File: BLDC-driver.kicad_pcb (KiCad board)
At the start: 2 copper layers, 52.2 x 52.2 mm, 105 parts, among them J1 Conn_01x06, J2 Conn_01x06, Q1 FDMS8018, Q2 FDMS8018, Q3 FDMS8018, Q4 FDMS8018, Q5 FDMS8018, Q6 FDMS8018, Q7 BC807, U1 NCP81151B, U11 SN75176AD, U2 STM32L412CB, U4 NCP81151B, U5 NCP81151B, U6 MP2359, U7 MIC5504-3.3YM5, U8 NCS213RSQT2G, U9 NCS213RSQT2G, Y1 8MHz

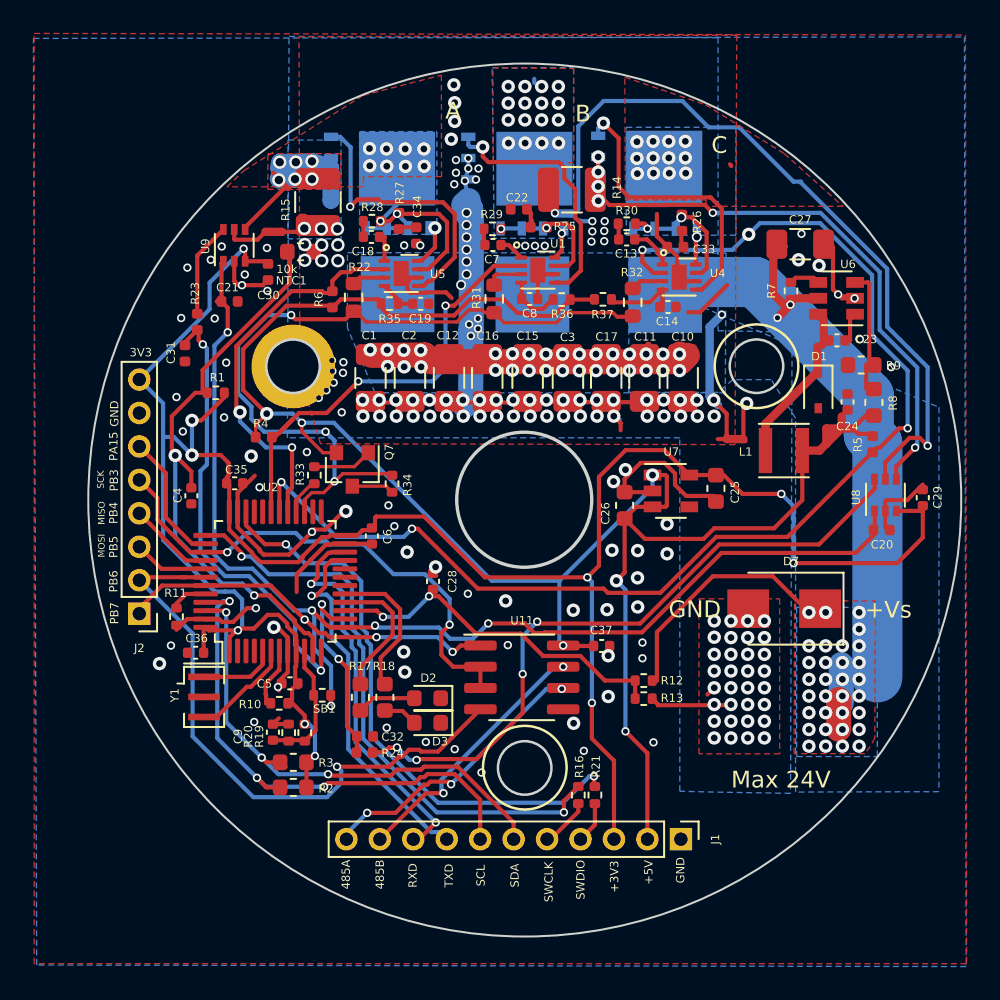
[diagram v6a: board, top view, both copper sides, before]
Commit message: Rev3: Update connectors, add JST PH connectors
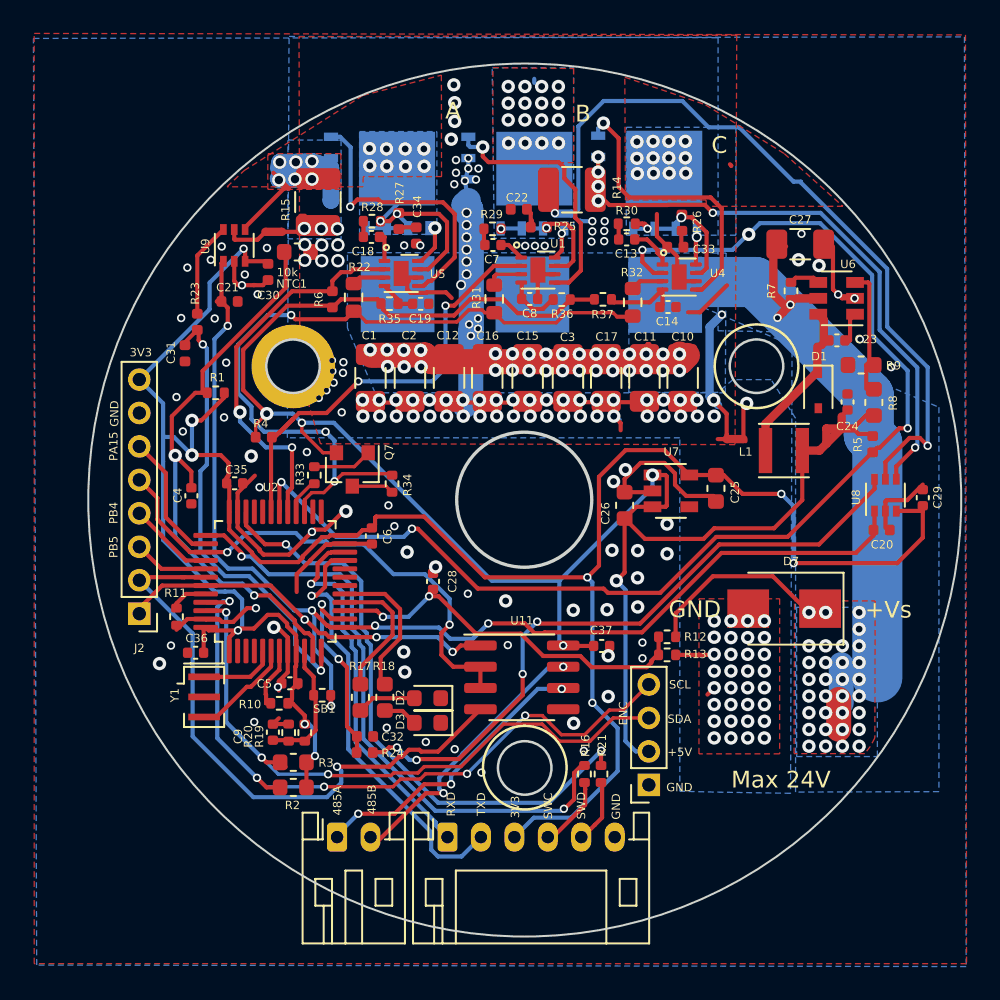
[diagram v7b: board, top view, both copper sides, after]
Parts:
- added J3: Conn_01x02, Connector_JST:JST_PH_S2B-PH-K_1x02_P2.00mm_Horizontal, F.Cu at (185.5, 143.3)
- added J4: Encoder, Connector_PinSocket_2.00mm:PinSocket_1x04_P2.00mm_Vertical, F.Cu at (204.1, 140.2)
- J1: footprint Connector_PinHeader_2.00mm:PinHeader_1x11_P2.00mm_Vertical -> Connector_JST:JST_PH_S6B-PH-K_1x06_P2.00mm_Horizontal
- moved J1 14.0 mm to (192.1, 143.3), turned to 0 degrees
- moved R12 2.97 mm to (205.2, 131.3)
- moved R13 2.97 mm to (205.2, 132.4)
- moved REF** 2.12 mm to (185.4, 131.8)
- moved R16 1.31 mm to (200.3, 139.5)
- moved R21 1.31 mm to (201.3, 139.5)
- moved NTC1 0.19 mm to (183.1, 108.3)
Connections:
- J1 pad 1: GND -> /RXD
- J1 pad 2: +5V -> /TXD
- J1 pad 6: /SDA -> GND
- R16 pad 2: Net-(J1-Pad5) -> Net-(J1-Pad4)
- R21 pad 2: Net-(J1-Pad4) -> Net-(J1-Pad5)
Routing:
- net /SCL: track 32.0 -> 42.3 mm, vias 3 -> 5
- net /SDA: track 30.2 -> 37.9 mm
- net +5V: track 119.3 -> 115.0 mm, vias 6 -> 5
- net +3V3: track 141.8 -> 146.1 mm
- net /TXD: track 22.2 -> 26.0 mm
- net +24V: track 87.6 -> 84.3 mm
- net GNDPWR: track 70.2 -> 67.9 mm
- net Net-(J1-Pad4): track 2.49 -> 4.52 mm
- net /VBUS: track 21.7 -> 23.1 mm
- net /SWCLK: track 35.3 -> 36.7 mm
- net /SWDIO: track 34.8 -> 36.2 mm
- net Net-(J1-Pad5): track 3.03 -> 3.99 mm
- net /CURR_B: track 40.5 -> 39.9 mm
- net /485A: track 17.0 -> 17.6 mm
- net /RXD: track 23.2 -> 22.7 mm, vias 2 -> 1
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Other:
- board text added: "ENC"
- board text added: "FOC Drive Walmis@2021.07 REV3 www.ensys.lt"
- board text added: "SWC"
- board text added: "SWD"
- board text removed: "FOC Drive Walmis@2021 REV2 www.ensys.lt"
- board text removed: "MISO"
- board text removed: "MOSI"
- board text removed: "PB3"
- board text removed: "PB6"
- board text removed: "PB7"
- board text removed: "SCK"
